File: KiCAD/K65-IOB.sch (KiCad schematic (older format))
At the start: 24 parts, among them J1 SBC6303 BUS, J2 PIO-A, J3 Conn_01x06, J4 PIO-B, U1 74HC139, U2 74HC04, U3 74HC74, U4 74HC125, U5 W65C51, U6 W65C22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

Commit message: シンボル間違い等修正
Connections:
- net labels removed: CA6, CA7
- no-connect marks 23 -> 33
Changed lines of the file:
@@
 	7750 5500 8000 5500
 Text Label 7750 5500 0    50   ~ 0
-CA6
+CA1
 Wire Wire Line
 	8500 5500 8750 5500
 Text Label 8600 5500 0    50   ~ 0
-CA7
+CA2
 $Comp
 L power:VCC #PWR024
@@
 Wire Wire Line
 	5300 3200 6300 3200
-Wire Wire Line
-	5400 3100 5400 3400
-Wire Wire Line
-	5400 3400 6300 3400
 Wire Wire Line
 	5500 3100 5500 3700
@@
 Wire Wire Line
 	4150 3250 4150 3500
+NoConn ~ 5400 3100
+NoConn ~ 1000 1050
+NoConn ~ 2100 1050
+NoConn ~ 1000 1750
+NoConn ~ 2100 1750
+NoConn ~ 1000 1850
+NoConn ~ 2100 1850
+NoConn ~ 1000 1950
+NoConn ~ 2100 1950
+NoConn ~ 1000 2050
+$Comp
+L power:PWR_FLAG #FLG0101
+U 1 1 5F4D2A2D
+P 4350 3500
+F 0 "#FLG0101" H 4350 3575 50  0001 C CNN
+F 1 "PWR_FLAG" V 4350 3628 50  0000 L CNN
+F 2 "" H 4350 3500 50  0001 C CNN
+F 3 "~" H 4350 3500 50  0001 C CNN
+	1    4350 3500
+	0    1    1    0
+$EndComp
+Wire Wire Line
+	4150 3500 4350 3500
+Connection ~ 4150 3500
+$Comp
+L power:PWR_FLAG #FLG0102
+U 1 1 5F4F2F87
+P 6050 4250
+F 0 "#FLG0102" H 6050 4325 50  0001 C CNN
+F 1 "PWR_FLAG" V 6050 4378 50  0000 L CNN
+F 2 "" H 6050 4250 50  0001 C CNN
+F 3 "~" H 6050 4250 50  0001 C CNN
+	1    6050 4250
+	0    1    1    0
+$EndComp
+Wire Wire Line
+	6000 4250 6050 4250
+Connection ~ 6000 4250
 $EndSCHEMATC

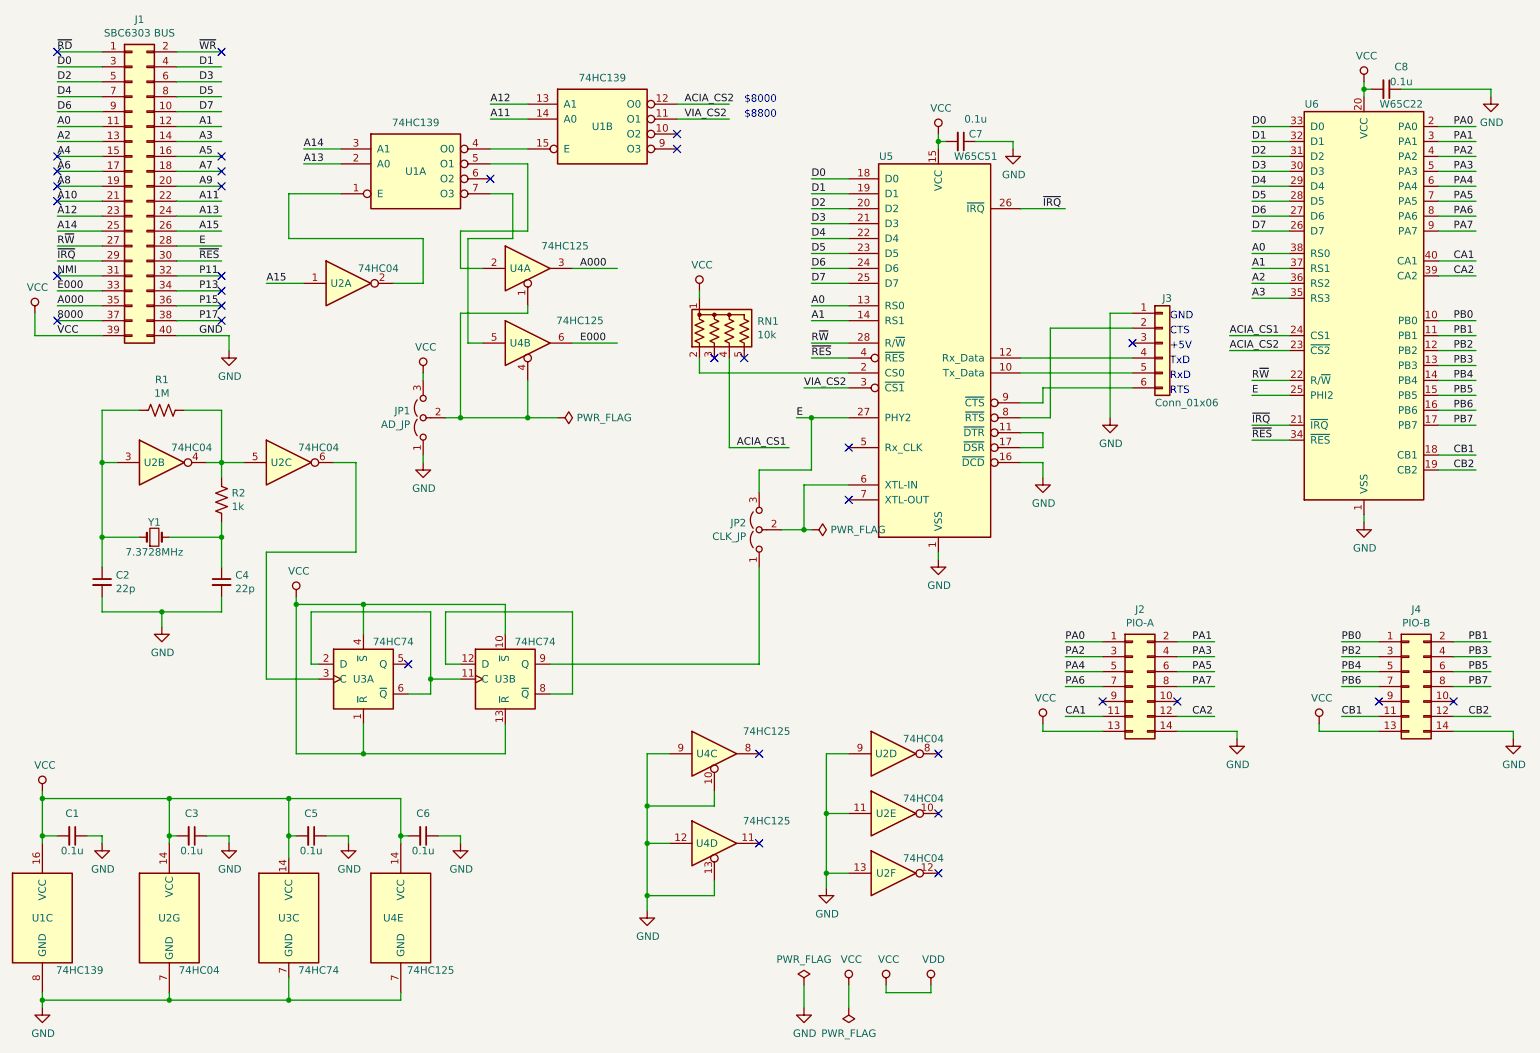
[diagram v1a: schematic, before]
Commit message: Lite版をMasterへ統合、UniversalMonitor W65C51対応点添付
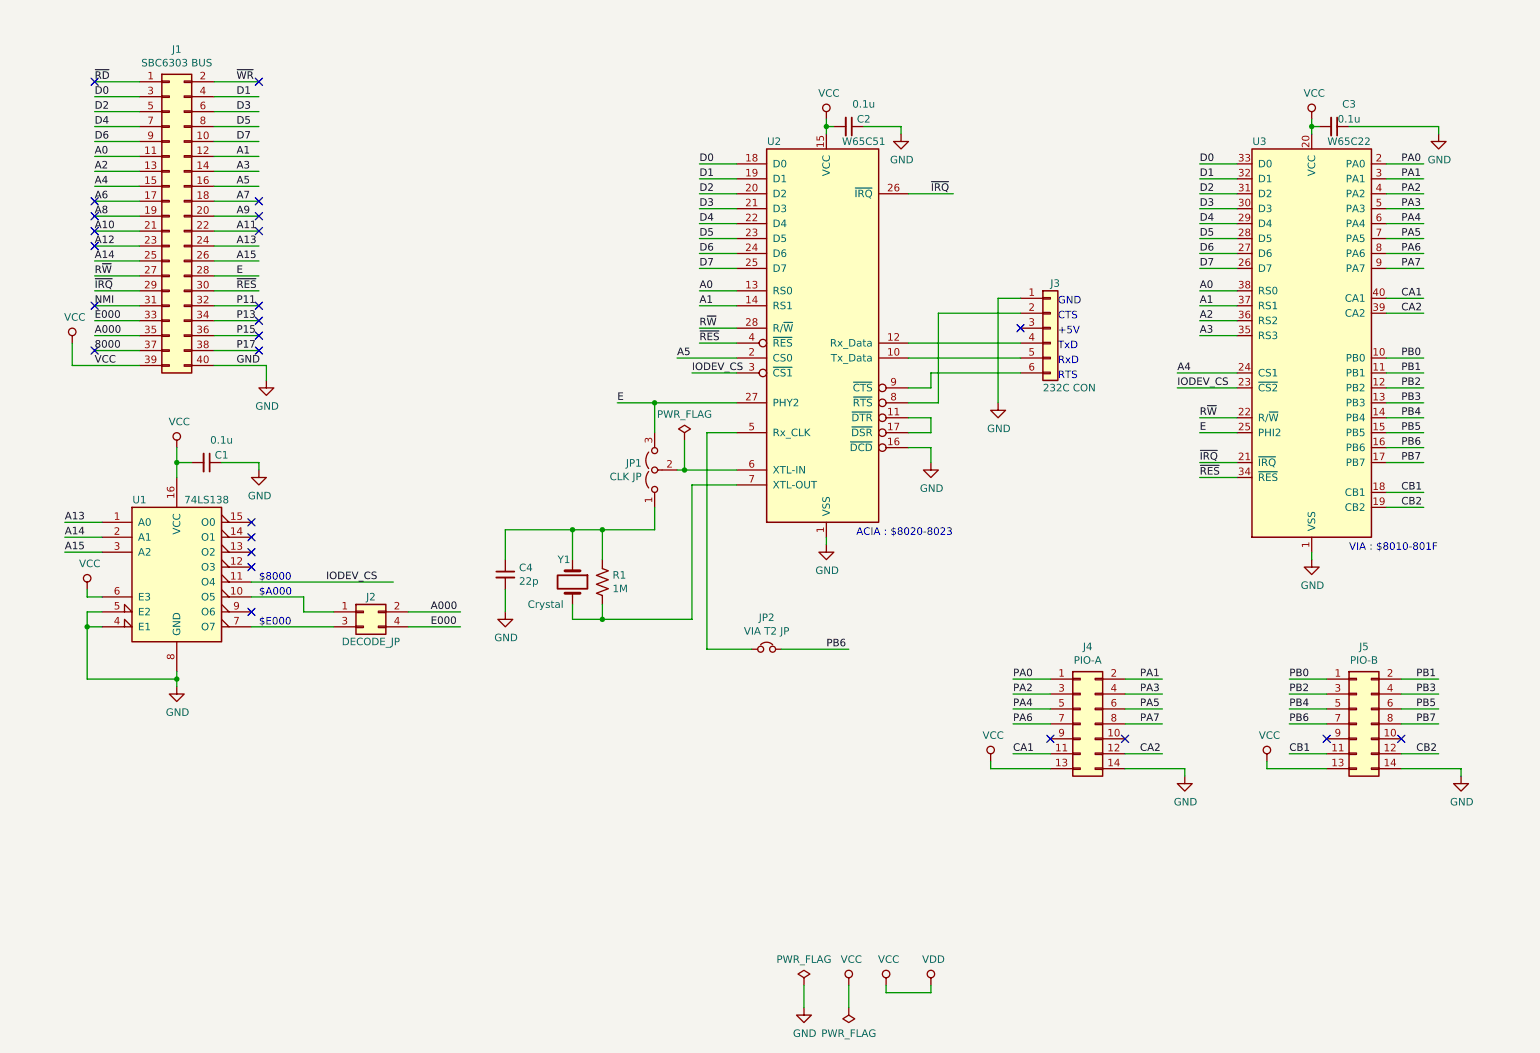
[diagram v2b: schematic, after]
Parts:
- removed C2: 22p, symbol Device:C_Small
- removed C3, C5, C6: 0.1u, symbol Device:C_Small
- removed JP2: CLK_JP, symbol Jumper:Jumper_3_Open
- removed R2: 1k, symbol Device:R_US
- removed RN1: 10k, Resistor_THT:R_Array_SIP5, symbol Device:R_Network04_US
- removed U1: 74HC139, symbol 74xx:74LS139
- removed U2: 74HC04, symbol 74xx:74HC04
- removed U3: 74HC74, symbol 74xx:74HC74
- removed U4: 74HC125, symbol 74xx:74LS125
- removed Y1: 7.3728MHz, symbol Device:Crystal_Small
- added J2: DECODE_JP, symbol Connector_Generic:Conn_02x02_Odd_Even
- added JP2: VIA T2 JP, symbol Device:Jumper_NC_Small
- added U1: 74LS138, symbol 74xx:74LS138
- added Y1: Crystal, symbol Device:Crystal
- J3: value Conn_01x06 -> 232C CON
- JP1: value AD_JP -> CLK JP
- renumbered C7 to C2, C8 to C3, J2 to J4, J4 to J5, U5 to U2, U6 to U3
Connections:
- net labels added: IODEV_CS
- net labels removed: ACIA_CS1, ACIA_CS2, VIA_CS2
- wire segments 298 -> 203
- no-connect marks 33 -> 25
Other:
- note added: "$A000"
- note added: "$E000"
- note added: "ACIA : $8020-8023"
- note added: "VIA : $8010-801F"
- note removed: "$8800"
- moved on the sheet: C2, C3, J1, J3, J4, J5, U2, U3

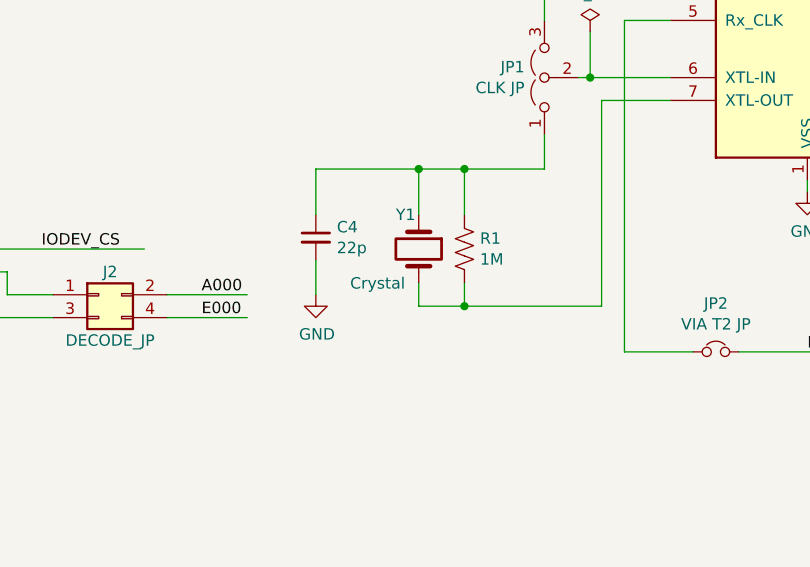
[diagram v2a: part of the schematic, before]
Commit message: パーツリスト追加、クリスタル周波数明示
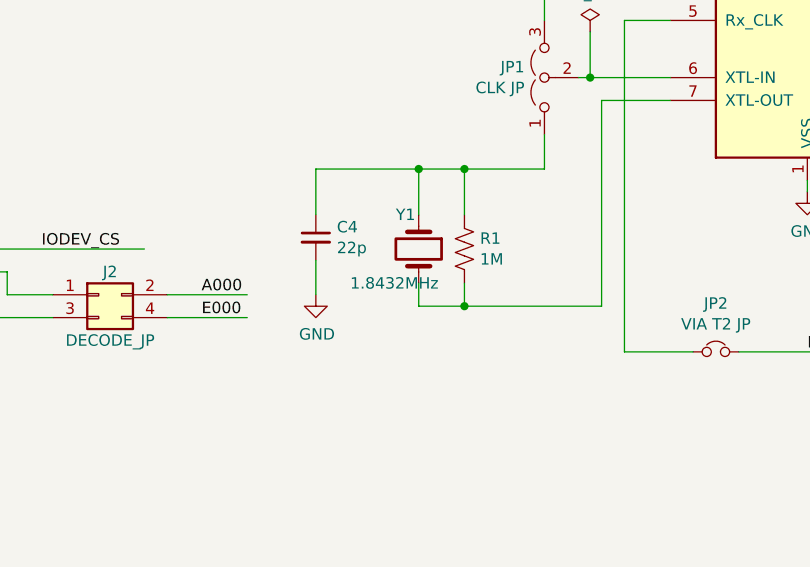
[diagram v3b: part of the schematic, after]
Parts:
- Y1: value Crystal -> 1.8432MHz
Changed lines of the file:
@@
 P 4450 4600
 F 0 "Y1" V 4300 4500 50  0000 L CNN
-F 1 "Crystal" V 4600 4300 50  0000 L CNN
+F 1 "1.8432MHz" V 4600 4300 50  0000 L CNN
 F 2 "" H 4450 4600 50  0001 C CNN
 F 3 "~" H 4450 4600 50  0001 C CNN

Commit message: 回路見直し、ガーバーデータ出力
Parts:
- removed J2: DECODE_JP, symbol Connector_Generic:Conn_02x02_Odd_Even
- removed JP1: CLK JP, symbol Jumper:Jumper_3_Open
- removed JP2: VIA T2 JP, symbol Device:Jumper_NC_Small
- added H1, H2, H3, H4: MountingHole, MountingHole:MountingHole_3.2mm_M3, symbol Mechanical:MountingHole
- added JP1: $A000 JP, Jumper:SolderJumper-2_P1.3mm_Open_RoundedPad1.0x1.5mm, symbol Jumper:SolderJumper_2_Open
- added JP2: $E000 JP, Jumper:SolderJumper-2_P1.3mm_Open_RoundedPad1.0x1.5mm, symbol Jumper:SolderJumper_2_Open
- added JP3: $8000 JP, Jumper:SolderJumper-3_P1.3mm_Bridged12_RoundedPad1.0x1.5mm, symbol Jumper:SolderJumper_3_Bridged12
- added JP4: CLK JP, Jumper:SolderJumper-3_P1.3mm_Bridged12_RoundedPad1.0x1.5mm, symbol Jumper:SolderJumper_3_Bridged12
- added JP5: EXT CLK JP, Jumper:SolderJumper-2_P1.3mm_Open_RoundedPad1.0x1.5mm, symbol Jumper:SolderJumper_2_Open
- C1: footprint (none) -> Capacitor_THT:C_Disc_D3.0mm_W1.6mm_P2.50mm
- C2: renamed from C4; footprint (none) -> Capacitor_THT:C_Disc_D3.0mm_W1.6mm_P2.50mm
- C3: renamed from C2; footprint (none) -> Capacitor_THT:C_Disc_D3.0mm_W1.6mm_P2.50mm
- C4: renamed from C3; footprint (none) -> Capacitor_THT:C_Disc_D3.0mm_W1.6mm_P2.50mm
- J1: footprint (none) -> Connector_PinHeader_2.54mm:PinHeader_2x20_P2.54mm_Horizontal
- J2: renamed from J3; footprint (none) -> Connector_PinHeader_2.54mm:PinHeader_1x06_P2.54mm_Horizontal
- J3: renamed from J4; footprint (none) -> Connector_PinHeader_2.54mm:PinHeader_2x07_P2.54mm_Vertical
- J4: renamed from J5; footprint (none) -> Connector_PinHeader_2.54mm:PinHeader_2x07_P2.54mm_Vertical
- R1: footprint (none) -> Resistor_THT:R_Axial_DIN0204_L3.6mm_D1.6mm_P7.62mm_Horizontal
- U1: footprint (none) -> Package_DIP:DIP-16_W7.62mm_Socket
- U2: footprint (none) -> Package_DIP:DIP-28_W15.24mm_Socket
- U3: footprint (none) -> Package_DIP:DIP-40_W15.24mm_Socket
- Y1: footprint (none) -> Crystal:Crystal_HC49-U_Vertical
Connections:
- wire segments 203 -> 210
- no-connect marks 25 -> 24
